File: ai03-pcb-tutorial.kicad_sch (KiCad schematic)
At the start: 14 parts

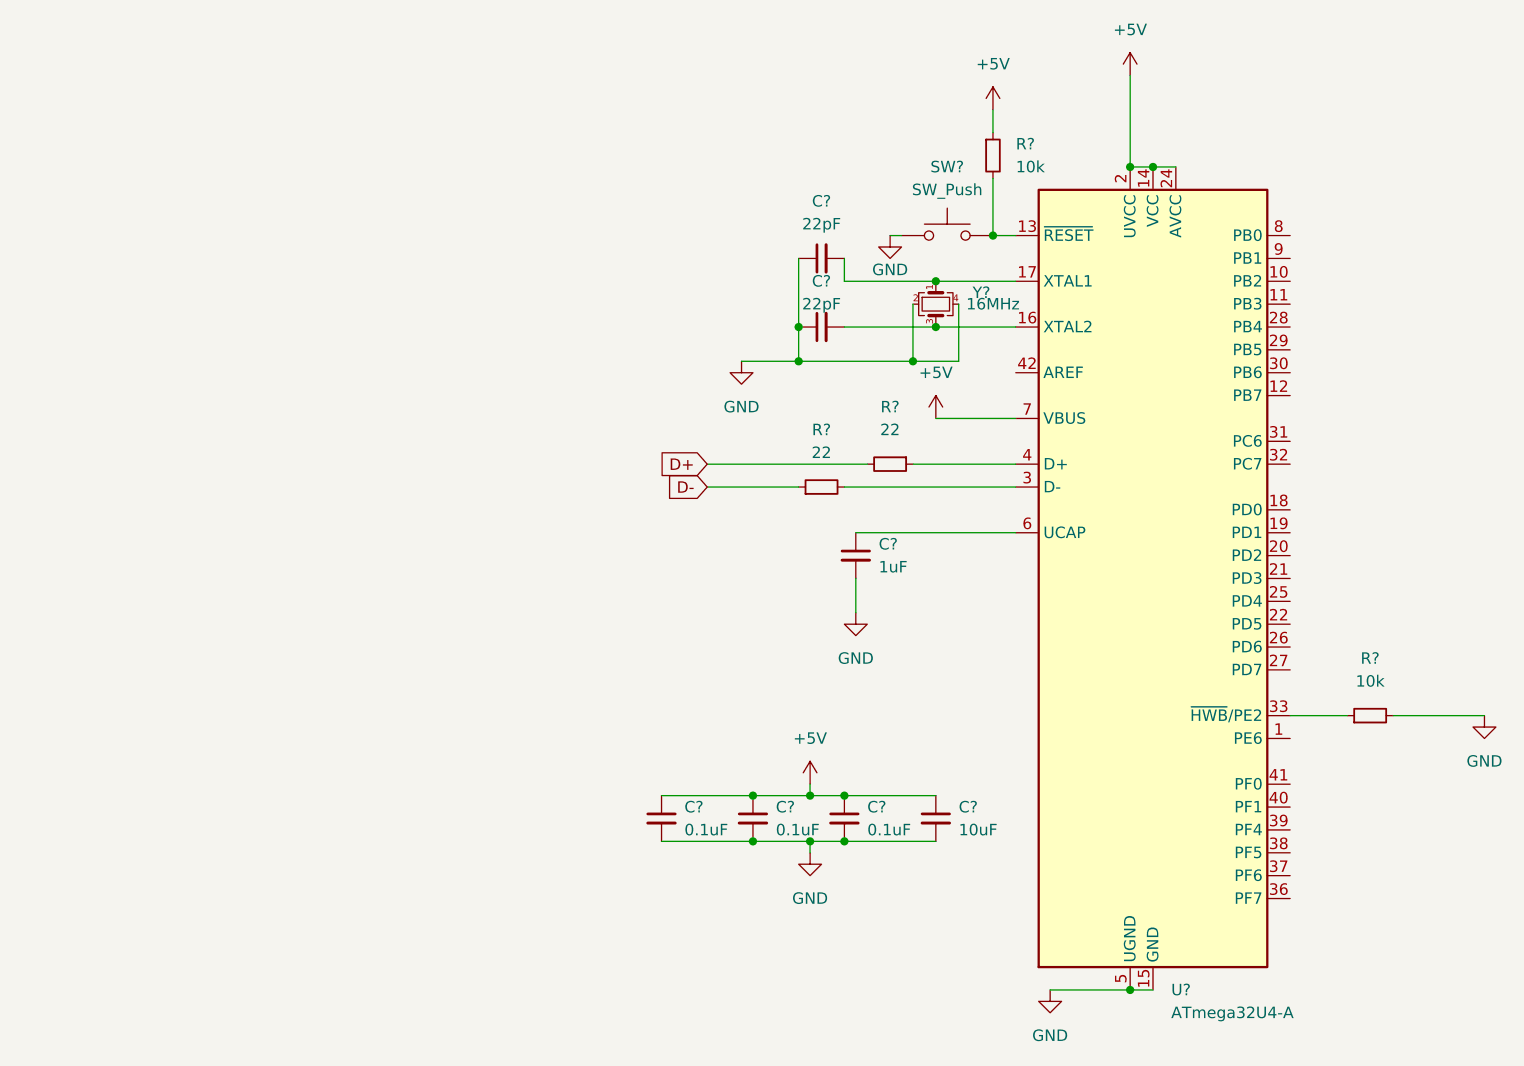
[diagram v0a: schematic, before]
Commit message: Add usb and 2x2 MX key schematic
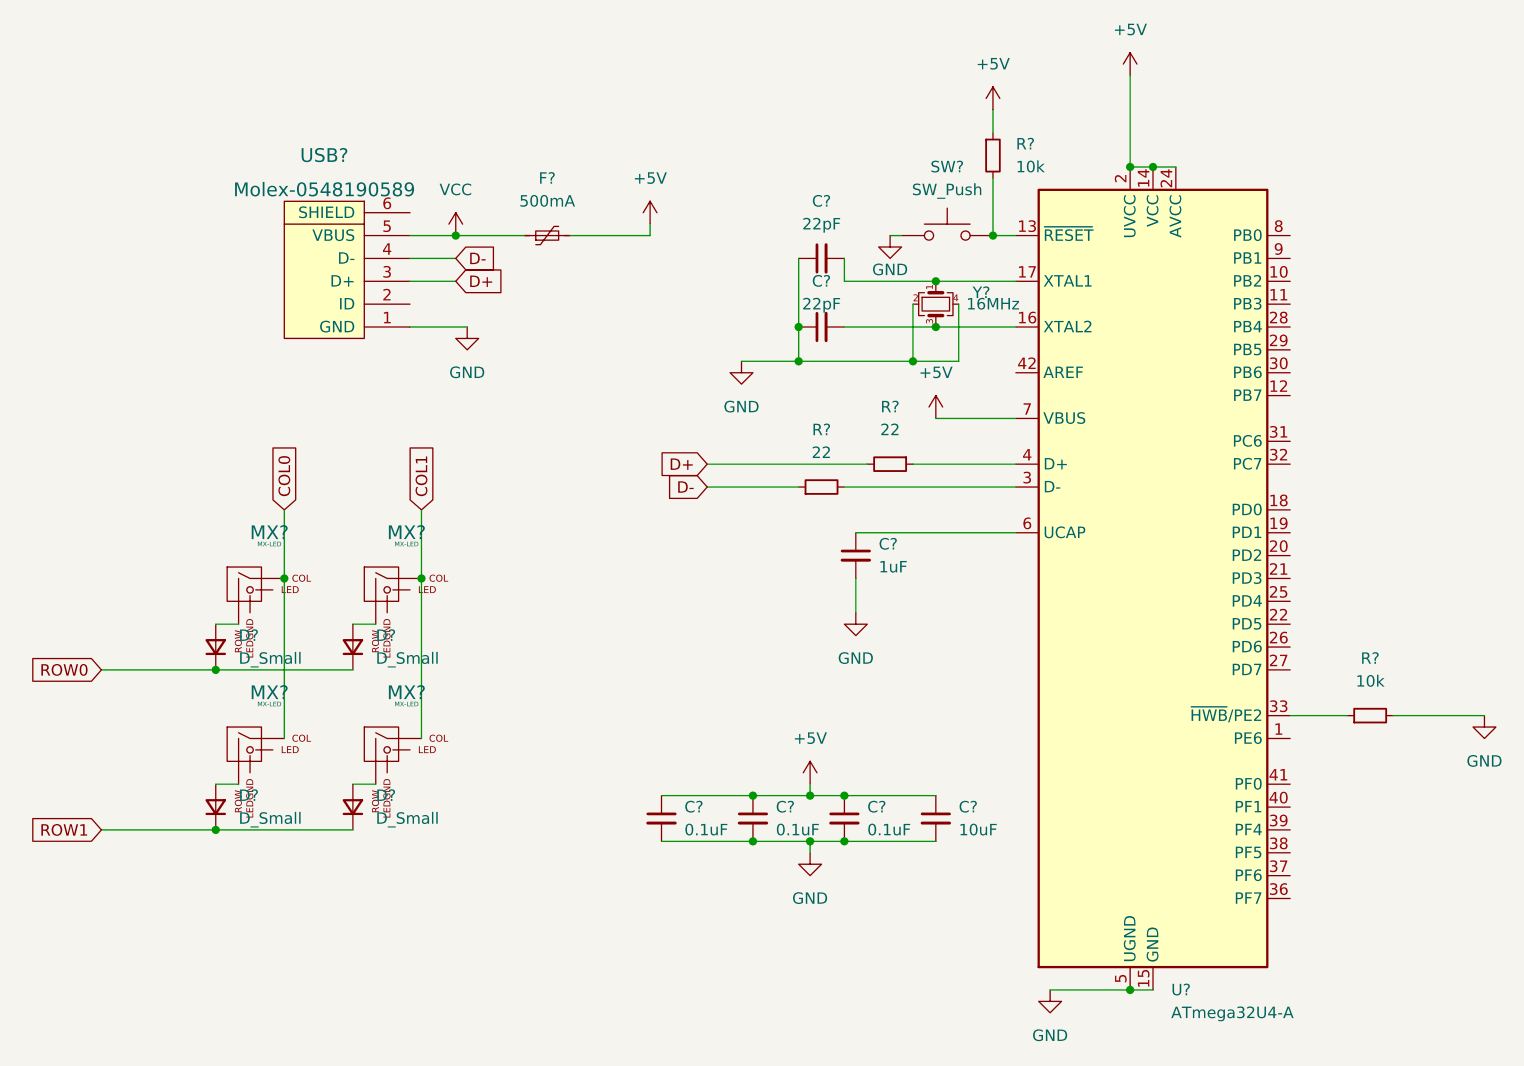
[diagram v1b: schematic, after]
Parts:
- added D? (x4): D_Small, symbol Device:D_Small
- added F?: 500mA, symbol Device:Polyfuse_Small
- added MX? (x4): MX-LED, symbol MX_Alps_Hybrid:MX-LED
- added USB?: Molex-0548190589, symbol random-keyboard-parts:Molex-0548190589
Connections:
- net +5V: now also F?.2
- net D+: now also USB?.3 (D+)
- net D-: now also USB?.4 (D-)
- net GND: now also USB?.1 (GND)
- new net: D?.2 (A), MX?.2 (ROW) (x4)
- new net COL0: MX?.1 (COL), MX?.1 (COL)
- new net COL1: MX?.1 (COL), MX?.1 (COL)
- new net ROW0: D?.1 (K), D?.1 (K)
- new net ROW1: D?.1 (K), D?.1 (K)
- new net VCC: F?.1, USB?.5 (VBUS)

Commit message: Add footprint bindings for all schematic items
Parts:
- C1, C2, C3, C4, C5, C6, C7: renamed from C?; footprint (none) -> Capacitor_SMD:C_0805_2012Metric
- D1, D2, D3, D4: renamed from D?; value D_Small -> SOD-123; footprint (none) -> Diode_SMD:D_SOD-123
- F1: renamed from F?; footprint (none) -> Fuse:Fuse_1206_3216Metric
- MX1, MX2, MX3, MX4: renamed from MX?; footprint (none) -> MX_Alps_Hybrid:MX-1U
- R1, R2, R3, R4: renamed from R?; footprint (none) -> Resistor_SMD:R_0805_2012Metric
- SW1: renamed from SW?; footprint (none) -> random-keyboard-parts:SKQG-1155865
- USB1: renamed from USB?; footprint (none) -> random-keyboard-parts:Molex-0548190589
- Y1: renamed from Y?; footprint (none) -> Crystal:Crystal_SMD_3225-4Pin_3.2x2.5mm
- gave numbers to parts that had none: 1
